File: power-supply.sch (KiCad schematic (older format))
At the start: 18 parts

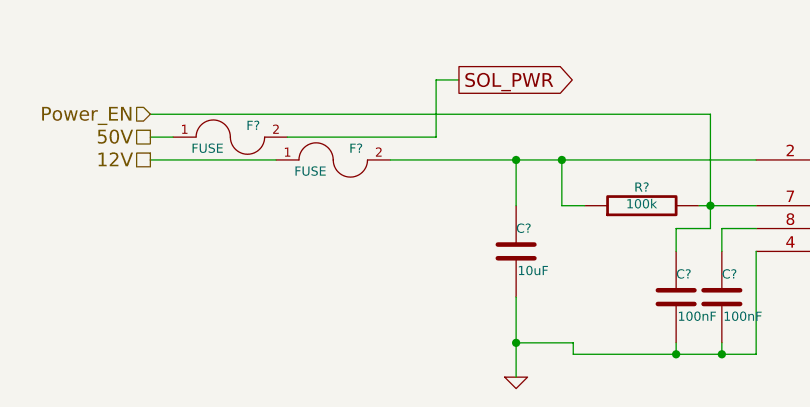
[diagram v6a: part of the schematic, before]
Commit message: added the other two current sense outputs and modified the power circut, i cant seem to add the 9th pad, the bottom thermal pad????
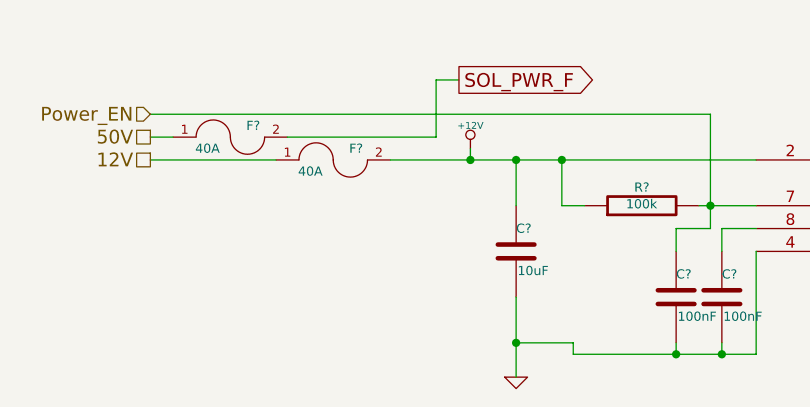
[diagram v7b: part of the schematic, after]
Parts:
- removed U?: RT7247AHGSP, symbol RT7247AHGSP
- added U?: RT7247AHGSP, ~, symbol RT7247AHGSP
- F? (x2): value FUSE -> 40A
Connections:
- net GND: now also U?.4 (GND)
- net Power_EN: now also U?.7 (EN)
- net +12V: now reaches C?.1, F?.2, R?.1
- net +12V: now also U?.2 (VIN)
- net at C?.1: now also U?.8 (SS)
- net at C?.1, D?.2 (K): now also U?.1 (Boot)
- net at C?.2, L?.1: now also U?.3 (SW)
- net at R?.1, R?.2: now also U?.5 (FB)
- net at C?.1, C?.1: now also U?.6 (COMP)
- net SOL_PWR renamed SOL_PWR_F
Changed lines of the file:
@@
-EESchema Schematic File Version 2  date 4/16/2013 12:48:50 AM
+EESchema Schematic File Version 2  date 4/16/2013 2:34:18 AM
 LIBS:power
 LIBS:device
@@
 $Descr A4 11693 8268
 encoding utf-8
-Sheet 6 8
+Sheet 6 10
 Title ""
 Date "16 apr 2013"
@@
 Text HLabel 1400 2950 0    60   Input ~ 0
 Power_EN
-Wire Wire Line
-	3000 3750 3000 4100
-Wire Wire Line
-	3000 3350 3000 3150
-Wire Wire Line
-	3900 3550 3900 3450
-Wire Wire Line
-	3900 3450 4050 3450
-Wire Wire Line
-	4050 4000 4050 3550
-Wire Wire Line
-	3000 3950 3250 3950
-Wire Wire Line
-	3250 4000 4050 4000
-Wire Wire Line
-	3900 4000 3900 3950
-Connection ~ 3000 3950
-Wire Wire Line
-	5300 3600 5300 3550
-Wire Wire Line
-	5250 3550 5550 3550
-Wire Wire Line
-	5550 3550 5550 3600
-Connection ~ 5300 3550
-Wire Wire Line
-	5550 4600 5550 4000
-Wire Wire Line
-	5300 4600 5550 4600
-Wire Wire Line
-	5300 4600 5300 4550
-Wire Wire Line
-	5300 4050 5300 4000
-Wire Wire Line
-	5250 3300 5950 3300
-Wire Wire Line
-	5250 3450 5800 3450
-Wire Wire Line
-	5800 4000 6650 4000
-Wire Wire Line
-	6650 3900 6650 4100
-Connection ~ 6650 4000
-Wire Wire Line
-	6650 3400 6650 3300
-Wire Wire Line
-	6550 3300 7250 3300
-Wire Wire Line
-	5800 3450 5800 4000
-Wire Wire Line
-	5250 3150 5350 3150
-Wire Wire Line
-	5800 3150 5750 3150
-Wire Wire Line
-	5800 3300 5800 3150
-Connection ~ 5800 3300
-Wire Wire Line
-	6650 4750 6650 4600
-Wire Wire Line
-	5400 4750 5400 4600
-Connection ~ 5400 4600
-Connection ~ 6650 3300
-Wire Wire Line
-	7000 3850 7000 3800
-Wire Wire Line
-	7150 3300 7150 3200
-Wire Wire Line
-	7000 3400 7000 3300
-Connection ~ 7000 3300
-Connection ~ 7150 3300
-Wire Wire Line
-	7850 2950 7850 2850
-Wire Wire Line
-	7850 2850 7650 2850
-Wire Wire Line
-	7650 2850 7650 3000
-Wire Wire Line
-	8050 3300 8150 3300
-Wire Wire Line
-	8150 3200 8150 3350
-Wire Wire Line
-	8150 3850 8150 3750
-Connection ~ 8150 3300
-Wire Wire Line
-	3300 3350 3200 3350
-Wire Wire Line
-	3200 3350 3200 3150
-Connection ~ 3200 3150
-Wire Wire Line
-	3800 3350 4050 3350
-Wire Wire Line
-	5300 3100 5300 3150
-Connection ~ 5300 3150
-Wire Wire Line
-	5300 2700 5300 2650
-Wire Wire Line
-	3250 3950 3250 4000
-Connection ~ 3900 4000
-Wire Wire Line
-	3700 3950 3700 4000
-Connection ~ 3700 4000
-Wire Wire Line
-	3700 3550 3700 3450
-Wire Wire Line
-	3700 3450 3850 3450
-Wire Wire Line
-	3850 3450 3850 2950
-Connection ~ 3850 3350
-Wire Wire Line
-	3850 2950 1400 2950
-Connection ~ 3000 3150
-Wire Wire Line
-	2650 3050 2650 2800
 Text GLabel 2750 2800 2    60   Output ~ 0
-SOL_PWR
-Wire Wire Line
-	2650 2800 2750 2800
+SOL_PWR_F
 $Comp
 L FUSE F?
@@
 P 1750 3050
 F 0 "F?" H 1850 3100 40  0000 C CNN
-F 1 "FUSE" H 1650 3000 40  0000 C CNN
+F 1 "40A" H 1650 3000 40  0000 C CNN
 F 2 "~" H 1750 3050 60  0000 C CNN
 F 3 "~" H 1750 3050 60  0000 C CNN
@@
 	1    0    0    -1
 $EndComp
-Wire Wire Line
-	4050 3150 2450 3150
 $Comp
 L FUSE F?
@@
 P 2200 3150
 F 0 "F?" H 2300 3200 40  0000 C CNN
-F 1 "FUSE" H 2100 3100 40  0000 C CNN
+F 1 "40A" H 2100 3100 40  0000 C CNN
 F 2 "~" H 2200 3150 60  0000 C CNN
 F 3 "~" H 2200 3150 60  0000 C CNN
@@
 	1    0    0    -1
 $EndComp
-Wire Wire Line
-	1950 3150 1400 3150
-Wire Wire Line
-	1500 3050 1400 3050
-Wire Wire Line
-	2000 3050 2650 3050
 $Comp
 L RT7247AHGSP U?
-U 1 1 516D349F
+U 1 1 516D4B84
 P 4600 3350
 F 0 "U?" H 4350 3900 60  0000 C CNN
 F 1 "RT7247AHGSP" H 4600 4000 60  0000 C CNN
-F 2 "" H 4600 3350 60  0000 C CNN
-F 3 "" H 4600 3350 60  0000 C CNN
+F 2 "~" H 4600 3350 60  0000 C CNN
+F 3 "~" H 4600 3350 60  0000 C CNN
 	1    4600 3350
 	1    0    0    -1
 $EndComp
+$Comp
+L +12V #PWR?
+U 1 1 516D7A31
+P 2800 3100
+F 0 "#PWR?" H 2800 3050 20  0001 C CNN
+F 1 "+12V" H 2800 3200 30  0000 C CNN
+F 2 "" H 2800 3100 60  0000 C CNN
+F 3 "" H 2800 3100 60  0000 C CNN
+	1    2800 3100
+	1    0    0    -1
+$EndComp
+Wire Wire Line
+	3000 3750 3000 4100
+Wire Wire Line
+	3000 3350 3000 3150
+Wire Wire Line
+	3900 3550 3900 3450
+Wire Wire Line
+	3900 3450 4050 3450
+Wire Wire Line
+	4050 4000 4050 3550
+Wire Wire Line
+	3000 3950 3250 3950
+Wire Wire Line
+	3250 4000 4050 4000
+Wire Wire Line
+	3900 4000 3900 3950
+Connection ~ 3000 3950
+Wire Wire Line
+	5300 3600 5300 3550
+Wire Wire Line
+	5250 3550 5550 3550
+Wire Wire Line
+	5550 3550 5550 3600
+Connection ~ 5300 3550
+Wire Wire Line
+	5550 4600 5550 4000
+Wire Wire Line
+	5300 4600 5550 4600
+Wire Wire Line
+	5300 4600 5300 4550
+Wire Wire Line
+	5300 4050 5300 4000
+Wire Wire Line
+	5250 3300 5950 3300
+Wire Wire Line
+	5250 3450 5800 3450
+Wire Wire Line
+	5800 4000 6650 4000
+Wire Wire Line
+	6650 3900 6650 4100
+Connection ~ 6650 4000
+Wire Wire Line
+	6650 3400 6650 3300
+Wire Wire Line
+	6550 3300 7250 3300
+Wire Wire Line
+	5800 3450 5800 4000
+Wire Wire Line
+	5250 3150 5350 3150
+Wire Wire Line
+	5800 3150 5750 3150
+Wire Wire Line
+	5800 3300 5800 3150
+Connection ~ 5800 3300
+Wire Wire Line
+	6650 4750 6650 4600
+Wire Wire Line
+	5400 4750 5400 4600
+Connection ~ 5400 4600
+Connection ~ 6650 3300
+Wire Wire Line
+	7000 3850 7000 3800
+Wire Wire Line
+	7150 3300 7150 3200
+Wire Wire Line
+	7000 3400 7000 3300
+Connection ~ 7000 3300
+Connection ~ 7150 3300
+Wire Wire Line
+	7850 2950 7850 2850
+Wire Wire Line
+	7850 2850 7650 2850
+Wire Wire Line
+	7650 2850 7650 3000
+Wire Wire Line
+	8050 3300 8150 3300
+Wire Wire Line
+	8150 3200 8150 3350
+Wire Wire Line
+	8150 3850 8150 3750
+Connection ~ 8150 3300
+Wire Wire Line
+	3300 3350 3200 3350
+Wire Wire Line
+	3200 3350 3200 3150
+Connection ~ 3200 3150
+Wire Wire Line
+	3800 3350 4050 3350
+Wire Wire Line
+	5300 3100 5300 3150
+Connection ~ 5300 3150
+Wire Wire Line
+	5300 2700 5300 2650
+Wire Wire Line
+	3250 3950 3250 4000
+Connection ~ 3900 4000
+Wire Wire Line
+	3700 3950 3700 4000
+Connection ~ 3700 4000
+Wire Wire Line
+	3700 3550 3700 3450
+Wire Wire Line
+	3700 3450 3850 3450
+Wire Wire Line
+	3850 3450 3850 2950
+Connection ~ 3850 3350
+Wire Wire Line
+	3850 2950 1400 2950
+Connection ~ 3000 3150
+Wire Wire Line
+	2650 3050 2650 2800
+Wire Wire Line
+	2650 2800 2750 2800
+Wire Wire Line
+	4050 3150 2450 3150
+Wire Wire Line
+	1950 3150 1400 3150
+Wire Wire Line
+	1500 3050 1400 3050
+Wire Wire Line
+	2000 3050 2650 3050
+Wire Wire Line
+	2800 3100 2800 3150
+Connection ~ 2800 3150
 $EndSCHEMATC
